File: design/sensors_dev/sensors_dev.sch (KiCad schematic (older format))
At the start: 13 parts, among them J1 Conn_01x02, J2 Conn_01x15, J3 Conn_01x15, Q1 DMN65D8L, Q2 DMN65D8L, U1 LP2980AIM5-3.0

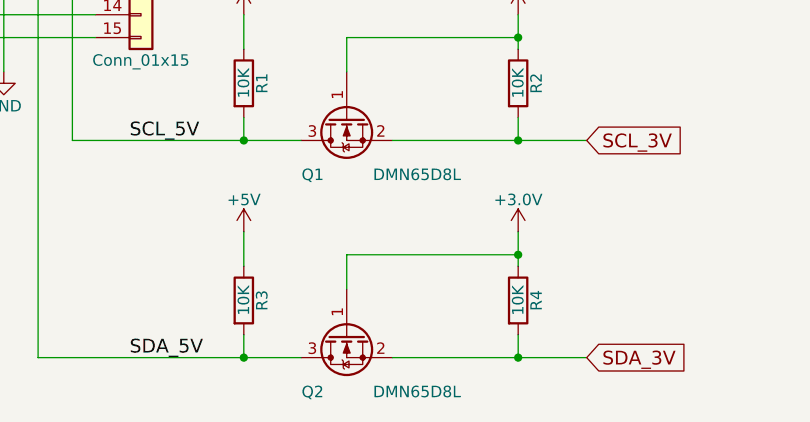
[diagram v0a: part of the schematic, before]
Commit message: fix FXAS21002 protocol and bidir mosfets
- Per review, tie pin 17 of FXAS21002 to HIGH the way it should be for
  I2C mode.
- switch out bidirectional mosfets for some that would actually work.
  (VGS_th too hih relative to VDS for the old ones)
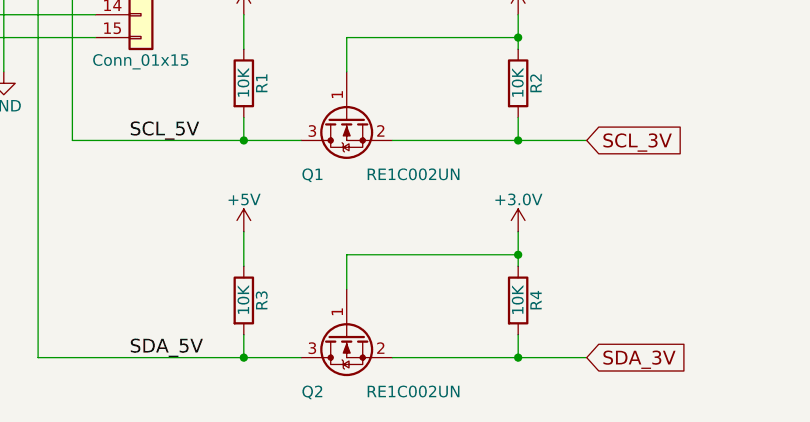
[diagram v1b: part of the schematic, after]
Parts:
- Q1, Q2: value DMN65D8L -> RE1C002UN
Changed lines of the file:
@@
 P 5100 5750
 F 0 "Q2" V 5350 5850 50  0000 L CNN
-F 1 "DMN65D8L" V 5350 5250 50  0000 L CNN
+F 1 "RE1C002UN" V 5350 5250 50  0000 L CNN
 F 2 "" H 5300 5850 50  0001 C CNN
 F 3 "" H 5100 5750 50  0001 C CNN
@@
 P 5100 4800
 F 0 "Q1" V 5350 4900 50  0000 L CNN
-F 1 "DMN65D8L" V 5350 4300 50  0000 L CNN
+F 1 "RE1C002UN" V 5350 4300 50  0000 L CNN
 F 2 "" H 5300 4900 50  0001 C CNN
 F 3 "" H 5100 4800 50  0001 C CNN

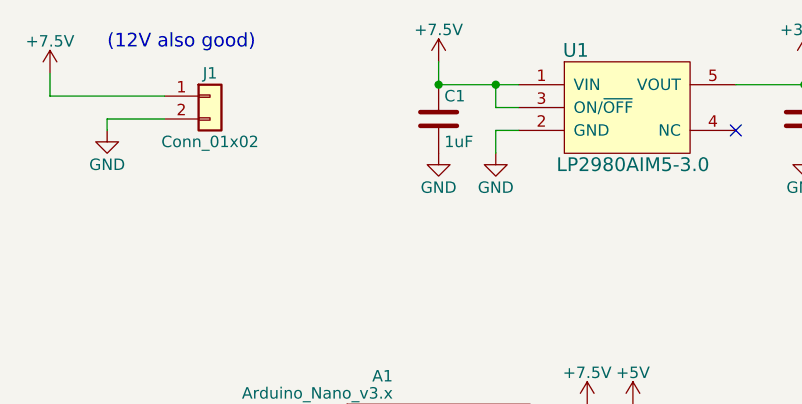
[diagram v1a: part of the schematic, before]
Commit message: Add footprints and decoupling caps to some ICs
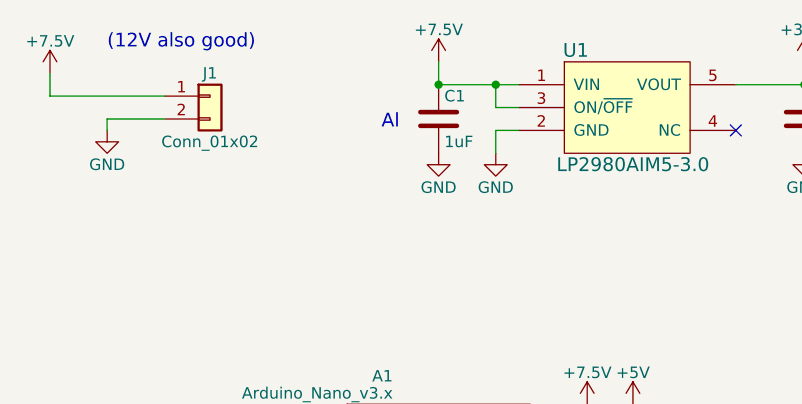
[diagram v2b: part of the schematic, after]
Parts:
- A1: footprint Flight_Instr:Arduino_Nano -> Module:Arduino_Nano
- C1, C2: footprint (none) -> Capacitors_ThroughHole:CP_Radial_Tantal_D5.0mm_P2.50mm
- J1: footprint (none) -> Pin_Headers:Pin_Header_Straight_1x02_Pitch2.54mm
- J2, J3: footprint (none) -> Pin_Headers:Pin_Header_Straight_1x15_Pitch2.54mm
- Q1, Q2: footprint (none) -> TO_SOT_Packages_SMD:SOT-23_Handsoldering
- R1, R2, R3, R4: footprint (none) -> Resistors_SMD:R_0805_HandSoldering
- U1: footprint (none) -> TO_SOT_Packages_THT:TO-92_Inline_Narrow_Oval
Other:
- note added: "Al"
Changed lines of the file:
@@
 F 0 "U1" H 3550 1700 60  0000 C CNN
 F 1 "LP2980AIM5-3.0" H 3800 1200 60  0000 C CNN
-F 2 "" H 3750 1500 60  0001 C CNN
+F 2 "TO_SOT_Packages_THT:TO-92_Inline_Narrow_Oval" H 3750 1500 60  0001 C CNN
 F 3 "" H 3750 1500 60  0001 C CNN
 	1    3800 1500
@@
 F 0 "C1" H 2975 1700 50  0000 L CNN
 F 1 "1uF" H 2975 1500 50  0000 L CNN
-F 2 "" H 2988 1450 50  0001 C CNN
+F 2 "Capacitors_ThroughHole:CP_Radial_Tantal_D5.0mm_P2.50mm" H 2988 1450 50  0001 C CNN
 F 3 "" H 2950 1600 50  0001 C CNN
 	1    2950 1600
@@
 F 0 "C2" H 4575 1700 50  0000 L CNN
 F 1 "2.2uF" H 4575 1500 50  0000 L CNN
-F 2 "" H 4588 1450 50  0001 C CNN
+F 2 "Capacitors_ThroughHole:CP_Radial_Tantal_D5.0mm_P2.50mm" H 4588 1450 50  0001 C CNN
 F 3 "" H 4550 1600 50  0001 C CNN
 	1    4550 1600
@@
 F 0 "A1" H 2750 4775 50  0000 R CNN
 F 1 "Arduino_Nano_v3.x" H 2750 4700 50  0000 R CNN
-F 2 "Flight_Instr:Arduino_Nano" H 3100 2800 50  0001 L CNN
+F 2 "Module:Arduino_Nano" H 3100 2800 50  0001 L CNN
 F 3 "" H 2950 2750 50  0001 C CNN
 	1    2950 3750
@@
 F 0 "J2" H 1700 4550 50  0000 C CNN
 F 1 "Conn_01x15" H 1700 2950 50  0000 C CNN
-F 2 "" H 1700 3750 50  0001 C CNN
+F 2 "Pin_Headers:Pin_Header_Straight_1x15_Pitch2.54mm" H 1700 3750 50  0001 C CNN
 F 3 "" H 1700 3750 50  0001 C CNN
 	1    1700 3750
@@
 F 0 "J3" H 4200 4550 50  0000 C CNN
 F 1 "Conn_01x15" H 4200 2950 50  0000 C CNN
-F 2 "" H 4200 3750 50  0001 C CNN
+F 2 "Pin_Headers:Pin_Header_Straight_1x15_Pitch2.54mm" H 4200 3750 50  0001 C CNN
 F 3 "" H 4200 3750 50  0001 C CNN
 	1    4200 3750
@@
 F 0 "J1" H 1950 1600 50  0000 C CNN
 F 1 "Conn_01x02" H 1950 1300 50  0000 C CNN
-F 2 "" H 1950 1500 50  0001 C CNN
+F 2 "Pin_Headers:Pin_Header_Straight_1x02_Pitch2.54mm" H 1950 1500 50  0001 C CNN
 F 3 "" H 1950 1500 50  0001 C CNN
 	1    1950 1500
@@
 F 0 "R1" V 4730 4650 50  0000 C CNN
 F 1 "10K" V 4650 4650 50  0000 C CNN
-F 2 "" V 4580 4650 50  0001 C CNN
+F 2 "Resistors_SMD:R_0805_HandSoldering" V 4580 4650 50  0001 C CNN
 F 3 "" H 4650 4650 50  0001 C CNN
 	1    4650 4650
@@
 F 0 "R2" V 5930 4650 50  0000 C CNN
 F 1 "10K" V 5850 4650 50  0000 C CNN
-F 2 "" V 5780 4650 50  0001 C CNN
+F 2 "Resistors_SMD:R_0805_HandSoldering" V 5780 4650 50  0001 C CNN
 F 3 "" H 5850 4650 50  0001 C CNN
 	1    5850 4650
@@
 F 0 "R3" V 4730 5600 50  0000 C CNN
 F 1 "10K" V 4650 5600 50  0000 C CNN
-F 2 "" V 4580 5600 50  0001 C CNN
+F 2 "Resistors_SMD:R_0805_HandSoldering" V 4580 5600 50  0001 C CNN
 F 3 "" H 4650 5600 50  0001 C CNN
 	1    4650 5600
@@
 F 0 "R4" V 5930 5600 50  0000 C CNN
 F 1 "10K" V 5850 5600 50  0000 C CNN
-F 2 "" V 5780 5600 50  0001 C CNN
+F 2 "Resistors_SMD:R_0805_HandSoldering" V 5780 5600 50  0001 C CNN
 F 3 "" H 5850 5600 50  0001 C CNN
 	1    5850 5600
@@
 F 0 "Q2" V 5350 5850 50  0000 L CNN
 F 1 "RE1C002UN" V 5350 5250 50  0000 L CNN
-F 2 "" H 5300 5850 50  0001 C CNN
+F 2 "TO_SOT_Packages_SMD:SOT-23_Handsoldering" H 5300 5850 50  0001 C CNN
 F 3 "" H 5100 5750 50  0001 C CNN
 	1    5100 5750
@@
 F 0 "Q1" V 5350 4900 50  0000 L CNN
 F 1 "RE1C002UN" V 5350 4300 50  0000 L CNN
-F 2 "" H 5300 4900 50  0001 C CNN
+F 2 "TO_SOT_Packages_SMD:SOT-23_Handsoldering" H 5300 4900 50  0001 C CNN
 F 3 "" H 5100 4800 50  0001 C CNN
 	1    5100 4800
@@
 Text Notes 1500 1300 0    60   ~ 0
 (12V also good)
+Text Notes 2700 1650 0    60   ~ 0
+Al
 $EndSCHEMATC

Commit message: Start PCB and swap out gyro
Old gyro (fxas) was 24 LGA and required a clearance between 3 and 4 mil,
which increases costs and cuts down fab house options. Swapped out the
gyro for another one with slightly higher drift but in a more convenient
package (LGA14).
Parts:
- U1: footprint TO_SOT_Packages_THT:TO-92_Inline_Narrow_Oval -> TO_SOT_Packages_SMD:SOT-23-5_HandSoldering
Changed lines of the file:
@@
 F 0 "U1" H 3550 1700 60  0000 C CNN
 F 1 "LP2980AIM5-3.0" H 3800 1200 60  0000 C CNN
-F 2 "TO_SOT_Packages_THT:TO-92_Inline_Narrow_Oval" H 3750 1500 60  0001 C CNN
+F 2 "TO_SOT_Packages_SMD:SOT-23-5_HandSoldering" H 3750 1500 60  0001 C CNN
 F 3 "" H 3750 1500 60  0001 C CNN
 	1    3800 1500

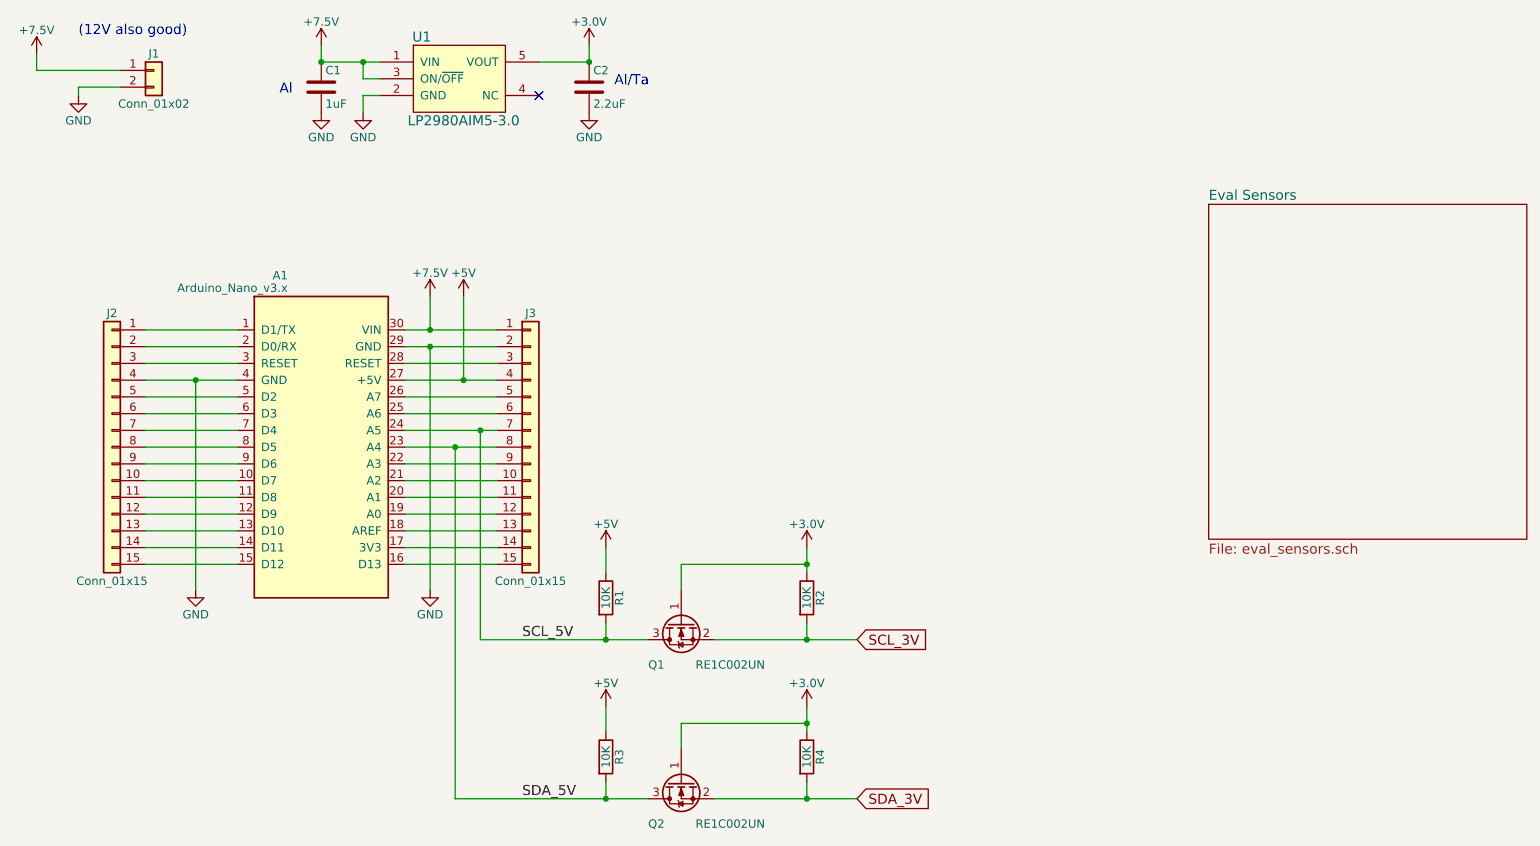
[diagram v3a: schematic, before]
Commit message: First pass board routing.
Also, remove arduino from PCB since this is a dev board and there's no
point paying for extra unused board space.
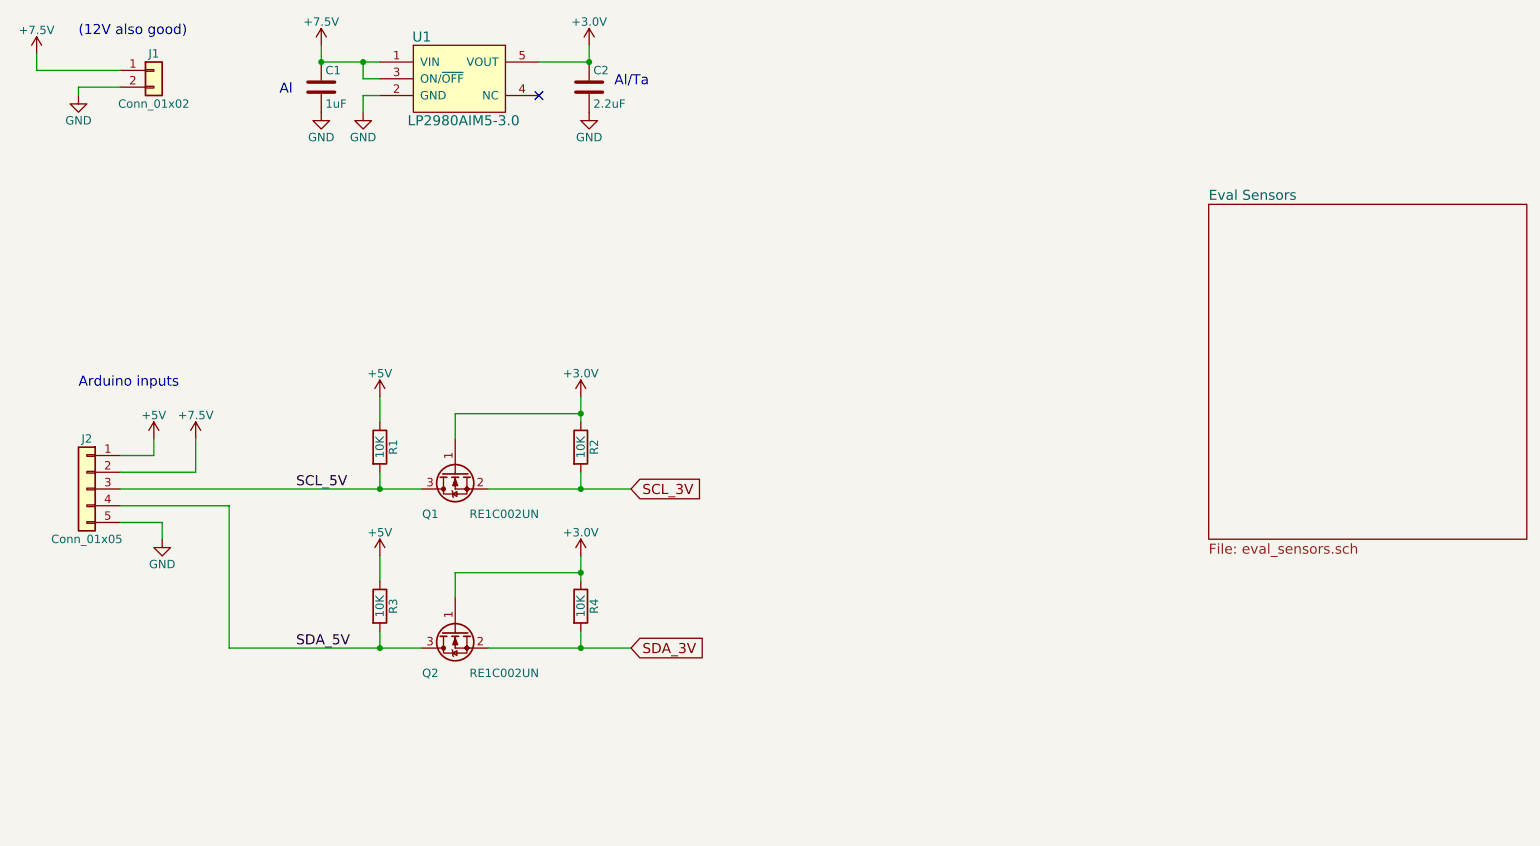
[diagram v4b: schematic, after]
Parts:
- removed A1: Arduino_Nano_v3.x, Module:Arduino_Nano, symbol Arduino_Nano_v3.x
- removed J2, J3: Conn_01x15, Pin_Headers:Pin_Header_Straight_1x15_Pitch2.54mm, symbol Conn_01x15
- added J2: Conn_01x05, Pin_Headers:Pin_Header_Straight_1x05_Pitch2.54mm, symbol Conn_01x05
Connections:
- net +5V: now also J2.1 (Pin_1)
- net +7.5V: now also J2.2 (Pin_2)
- net GND: now also J2.5 (Pin_5)
- net SCL_5V: now also J2.3 (Pin_3)
- net SDA_5V: now also J2.4 (Pin_4)
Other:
- note added: "Arduino inputs\n"
- moved on the sheet: Q1, Q2, R1, R2, R3, R4

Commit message: Redo board placement and routing
Will send to fab after final review.
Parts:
- R1, R2, R3, R4: footprint Resistors_SMD:R_0805_HandSoldering -> Resistors_SMD:R_0603_HandSoldering
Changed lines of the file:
@@
 F 0 "R1" V 3380 3750 50  0000 C CNN
 F 1 "10K" V 3300 3750 50  0000 C CNN
-F 2 "Resistors_SMD:R_0805_HandSoldering" V 3230 3750 50  0001 C CNN
+F 2 "Resistors_SMD:R_0603_HandSoldering" V 3230 3750 50  0001 C CNN
 F 3 "" H 3300 3750 50  0001 C CNN
 	1    3300 3750
@@
 F 0 "R2" V 4580 3750 50  0000 C CNN
 F 1 "10K" V 4500 3750 50  0000 C CNN
-F 2 "Resistors_SMD:R_0805_HandSoldering" V 4430 3750 50  0001 C CNN
+F 2 "Resistors_SMD:R_0603_HandSoldering" V 4430 3750 50  0001 C CNN
 F 3 "" H 4500 3750 50  0001 C CNN
 	1    4500 3750
@@
 F 0 "R3" V 3380 4700 50  0000 C CNN
 F 1 "10K" V 3300 4700 50  0000 C CNN
-F 2 "Resistors_SMD:R_0805_HandSoldering" V 3230 4700 50  0001 C CNN
+F 2 "Resistors_SMD:R_0603_HandSoldering" V 3230 4700 50  0001 C CNN
 F 3 "" H 3300 4700 50  0001 C CNN
 	1    3300 4700
@@
 F 0 "R4" V 4580 4700 50  0000 C CNN
 F 1 "10K" V 4500 4700 50  0000 C CNN
-F 2 "Resistors_SMD:R_0805_HandSoldering" V 4430 4700 50  0001 C CNN
+F 2 "Resistors_SMD:R_0603_HandSoldering" V 4430 4700 50  0001 C CNN
 F 3 "" H 4500 4700 50  0001 C CNN
 	1    4500 4700
